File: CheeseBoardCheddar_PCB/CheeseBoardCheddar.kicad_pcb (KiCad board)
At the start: 2 copper layers, 50 x 100 mm, 31 parts, among them P1 USB_Micro, P10 LOGO1, P11 LOGO2, P13 LOGO_CHEESE, P2 5V_EXT, P3 SERIAL_HC12, P4 S_SERIAL, P5 NODEMCU_1, P6 NODEMCU_2, P7 PCB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

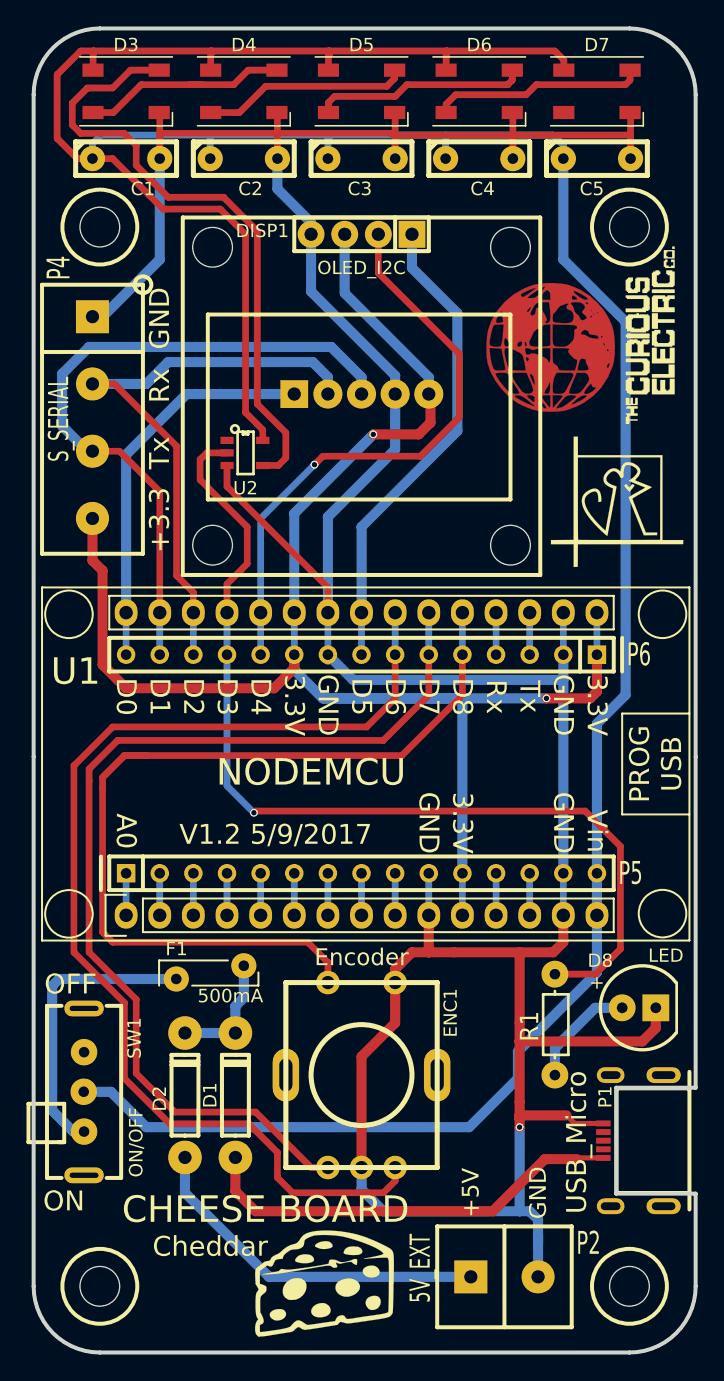
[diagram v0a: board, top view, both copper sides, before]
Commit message: Updated PCB with Encoder switch sorted
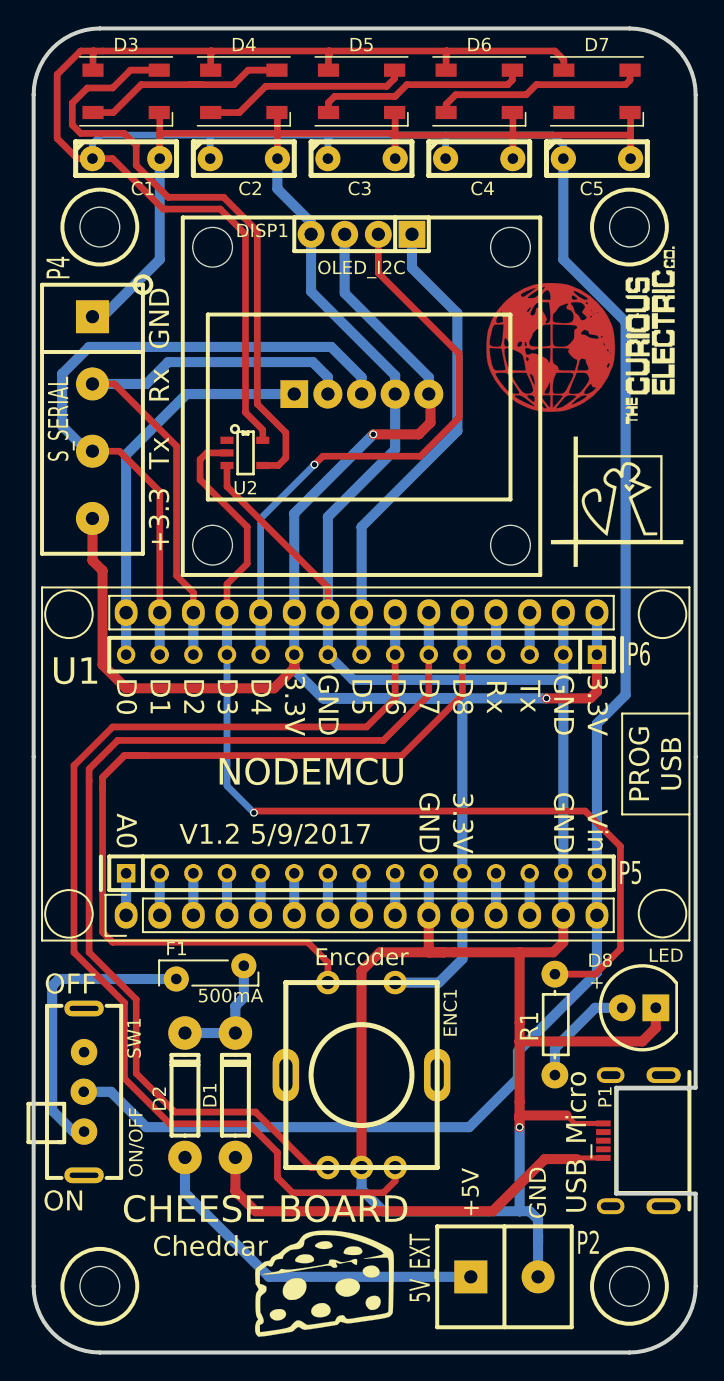
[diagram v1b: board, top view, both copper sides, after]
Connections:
- D7 pad 2: (no net) -> Net-(D7-Pad2)
- ENC1 pad 2: GND -> +3V3
- P1 pad 2: (no net) -> Net-(P1-Pad2)
- P1 pad 3: (no net) -> Net-(P1-Pad3)
- P1 pad 4: (no net) -> Net-(P1-Pad4)
- P10 pad 1: (no net) -> Net-(P10-Pad1)
- U2 pad 1: (no net) -> Net-(U2-Pad1)
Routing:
- net +3V3: track 127.1 -> 136.2 mm
- net GND: track 267.1 -> 269.3 mm
